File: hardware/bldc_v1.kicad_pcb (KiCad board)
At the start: 4 copper layers, 63 parts, among them J1 Conn_01x06, J2 1x2_ScrewTerminal_65A, J3 Screw_Terminal_01x05, J4 RJ45, J5 Screw_Terminal_01x03, M1 IPB044N15N5, M2 IPB044N15N5, M3 IPB044N15N5, M4 IPB044N15N5, M5 IPB044N15N5, M6 IPB044N15N5, M7 STM32F4-DISCOVERY, U1 AD8205, U2 AD8205

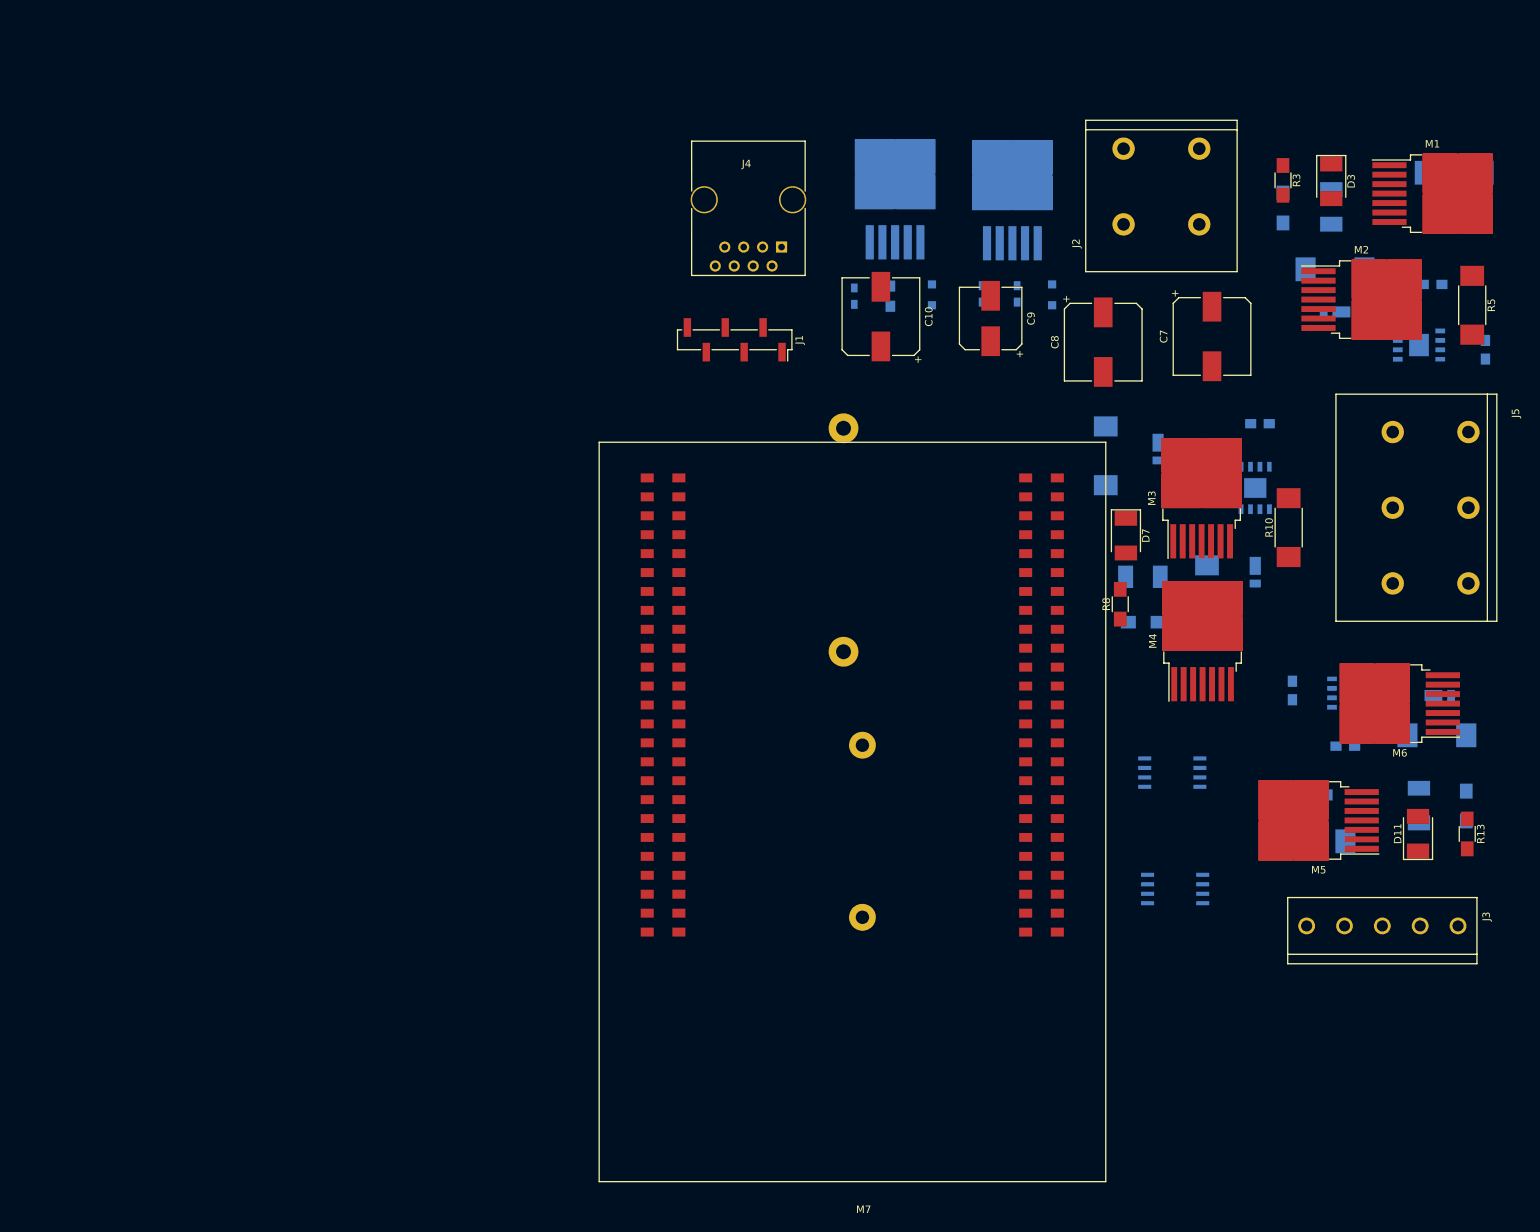
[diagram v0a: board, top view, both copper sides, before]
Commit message: routed phase A power electronics
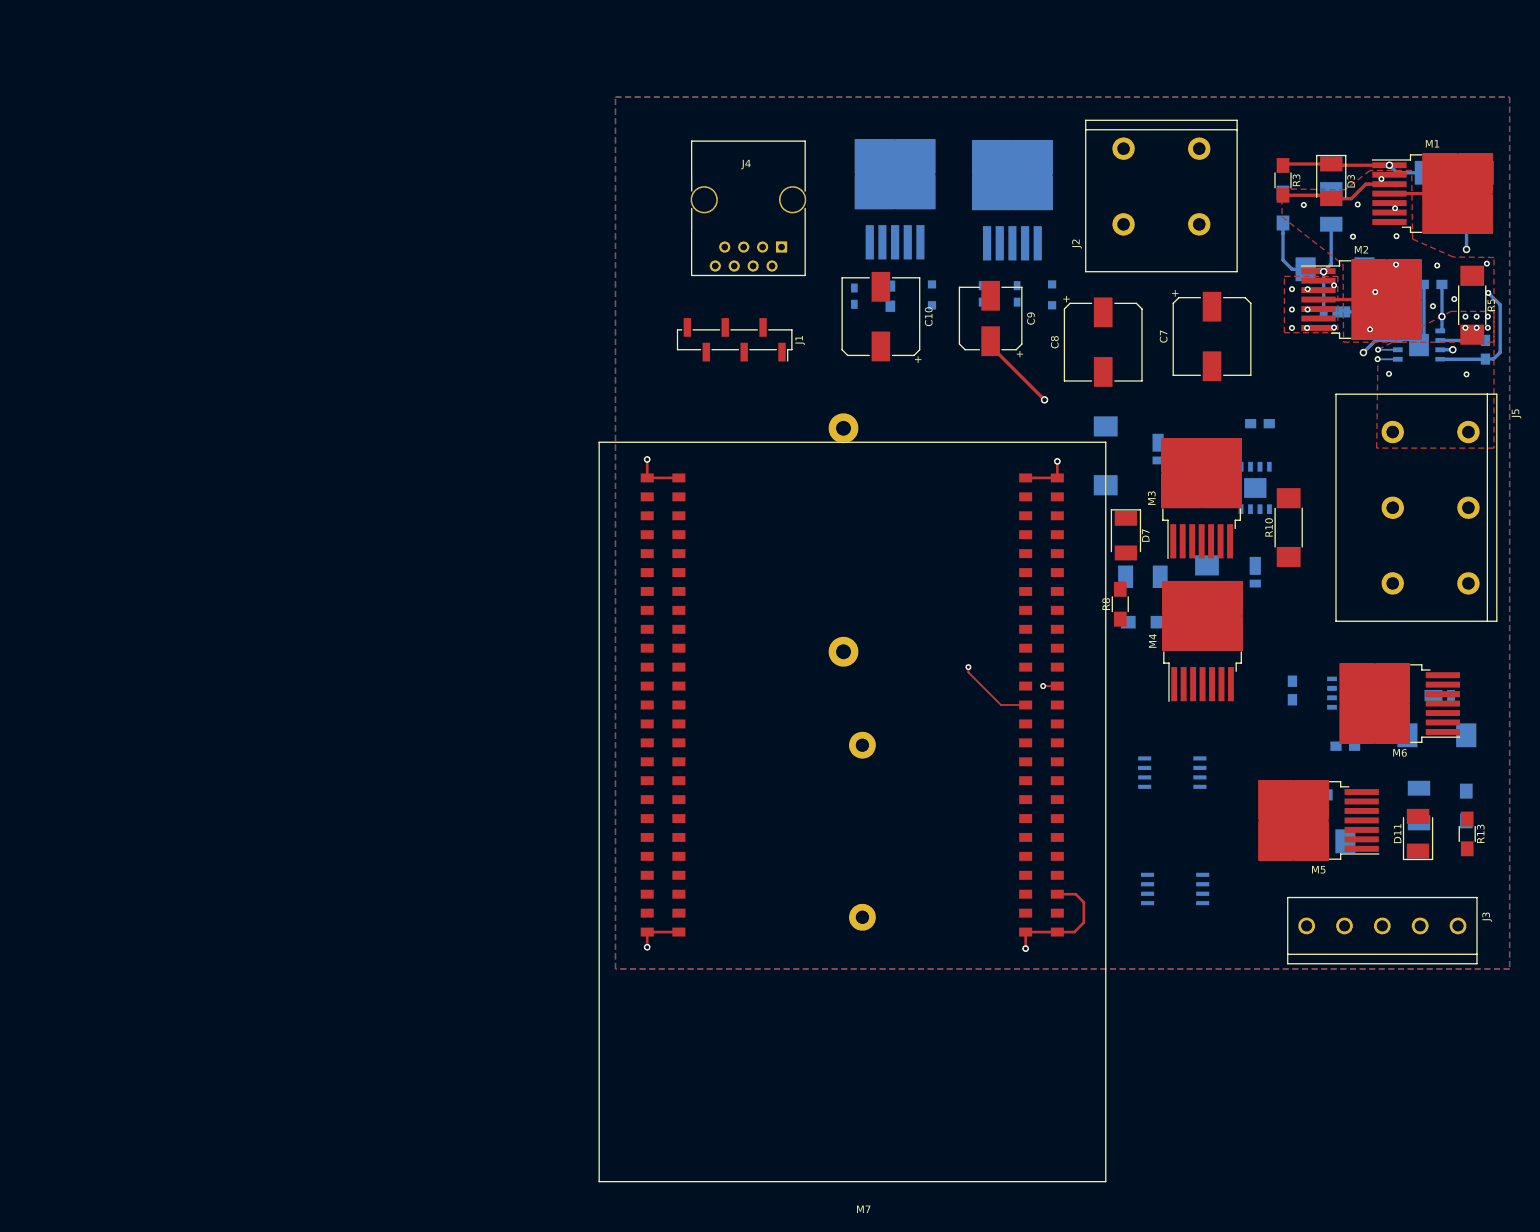
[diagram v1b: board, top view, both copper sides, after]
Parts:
- moved D1 0.28 mm to (228.0, 49.0)
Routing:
- net /GateDriver/LS_A_TTL_PWM: track 0.00 -> 102.0 mm, vias 0 -> 2
- net /GateDriver/HS_A_TTL_PWM: track 0.00 -> 101.4 mm, vias 0 -> 2
- net /GateDriver/+12V: track 0.00 -> 75.2 mm, vias 0 -> 2
- net /GND: track 0.00 -> 51.7 mm, vias 0 -> 13
- net /GateDriver/PhaseASource: track 0.00 -> 41.5 mm, vias 0 -> 14
- net /GateDriver/HS_A_GATE: track 0.00 -> 29.0 mm, vias 0 -> 2
- net Net-(D1-Pad2): track 0.00 -> 26.6 mm, vias 0 -> 1
- net Net-(D2-Pad2): track 0.00 -> 23.5 mm, vias 0 -> 1
- net /GateDriver/LS_A_GATE: track 0.00 -> 15.4 mm
- net /48v: track 0.00 -> 9.15 mm
- net Net-(C3-Pad1): track 0.00 -> 6.08 mm
- net /MOSFETS/PhaseA: vias 0 -> 8
- added copper zone on F.Cu, net /48v
- added copper zone on B.Cu, net /GND
- added copper zone on F.Cu, net /GND
- added copper zone on F.Cu, net /GateDriver/PhaseASource
- added copper zone on Inner2.Cu, net /GateDriver/PhaseASource
- added copper zone on F.Cu, net /MOSFETS/PhaseA
- added copper zone on Inner2.Cu, net /MOSFETS/PhaseA
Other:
- net class Large added: clearance 0.2, trace_width 0.45, via_dia 1, via_drill 0.6
- net class Medium added: clearance 0.2, trace_width 0.35, via_dia 0.9, via_drill 0.5
- net class Small added: clearance 0.2, trace_width 0.25, via_dia 0.8, via_drill 0.4

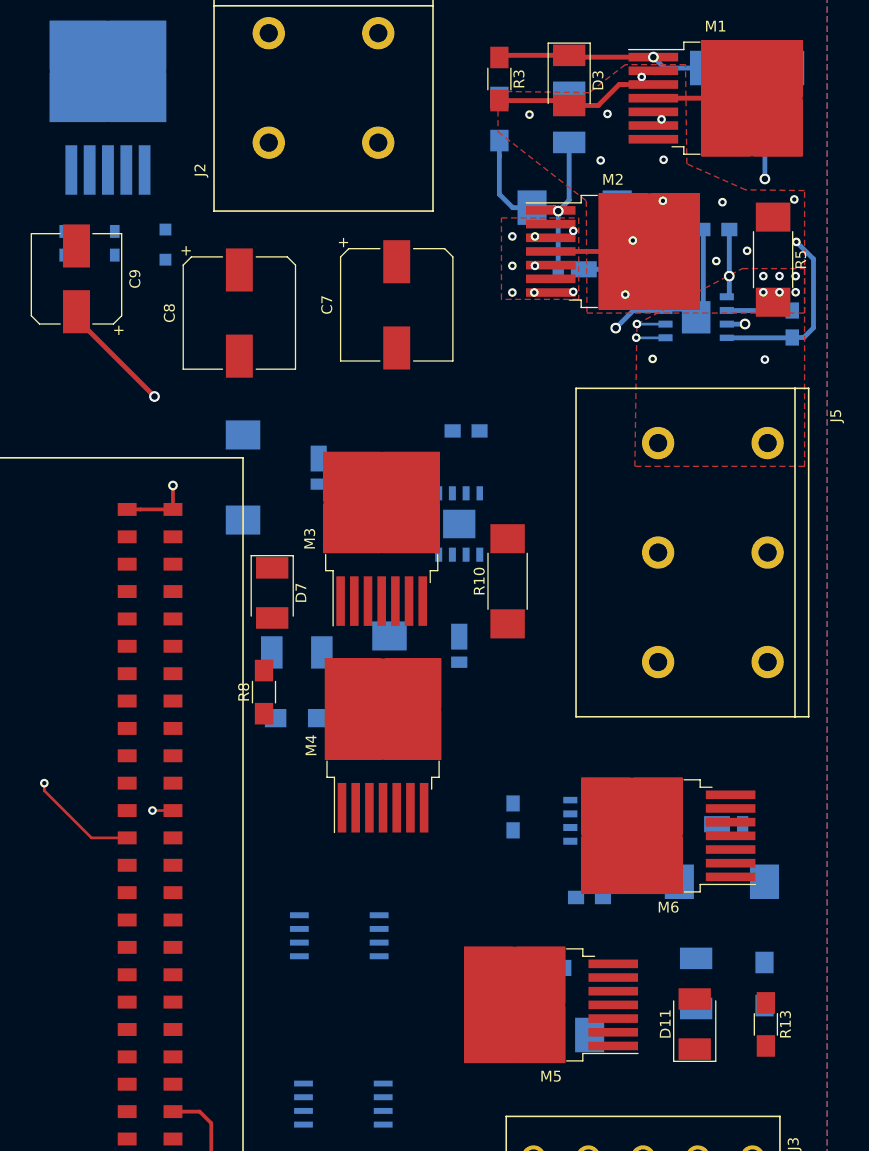
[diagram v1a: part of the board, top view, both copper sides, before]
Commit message: routed phase B power electronics
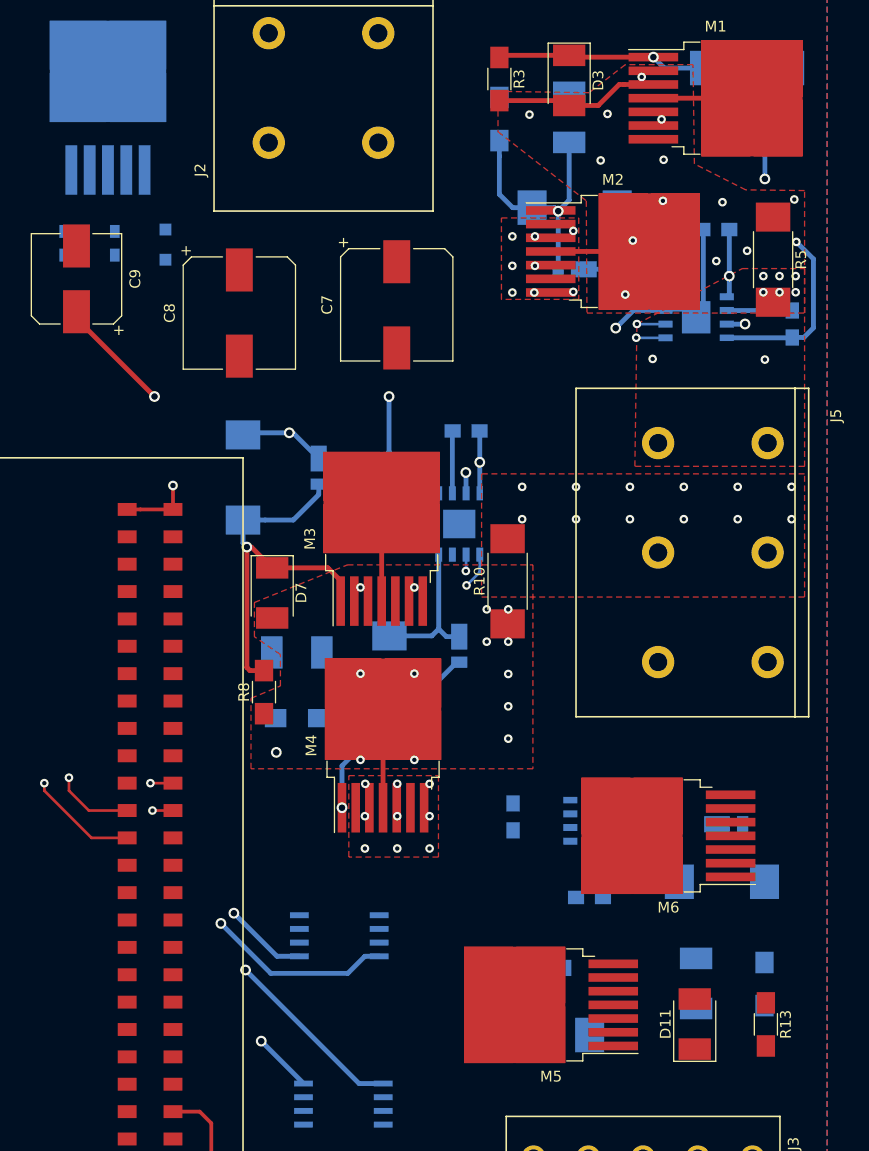
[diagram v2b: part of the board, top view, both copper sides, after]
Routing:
- net /GateDriver/PhaseASource: track 41.5 -> 145.9 mm, vias 14 -> 15
- net /MOSFETS/PhaseA: track 0.00 -> 92.6 mm, vias 8 -> 9
- net /MOSFETS/PhaseB: track 0.00 -> 90.9 mm, vias 0 -> 13
- net /GateDriver/HS_B_TTL_PWM: track 0.00 -> 65.2 mm, vias 0 -> 2
- net /GateDriver/LS_B_TTL_PWM: track 0.00 -> 64.1 mm, vias 0 -> 2
- net /GateDriver/PhaseBSource: track 0.00 -> 61.8 mm, vias 0 -> 16
- net Net-(D5-Pad2): track 0.00 -> 36.4 mm, vias 0 -> 1
- net Net-(D6-Pad2): track 0.00 -> 34.6 mm, vias 0 -> 1
- net /GateDriver/HS_B_GATE: track 0.00 -> 27.9 mm, vias 0 -> 2
- net /GateDriver/+12V: track 75.2 -> 90.4 mm, vias 2 -> 3
- net /GateDriver/LS_B_GATE: track 0.00 -> 13.9 mm
- net /48v: track 9.15 -> 18.3 mm
- net Net-(C1-Pad1): track 0.00 -> 5.80 mm
- net /GND: vias 13 -> 22
- added copper zone on F.Cu, net /GateDriver/PhaseBSource
- added copper zone on Inner2.Cu, net /GateDriver/PhaseBSource
- added copper zone on F.Cu, net /MOSFETS/PhaseB
- added copper zone on Inner2.Cu, net /MOSFETS/PhaseB
